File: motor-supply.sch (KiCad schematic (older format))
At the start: 16 parts, among them Q9 2N7002, U2 A8498

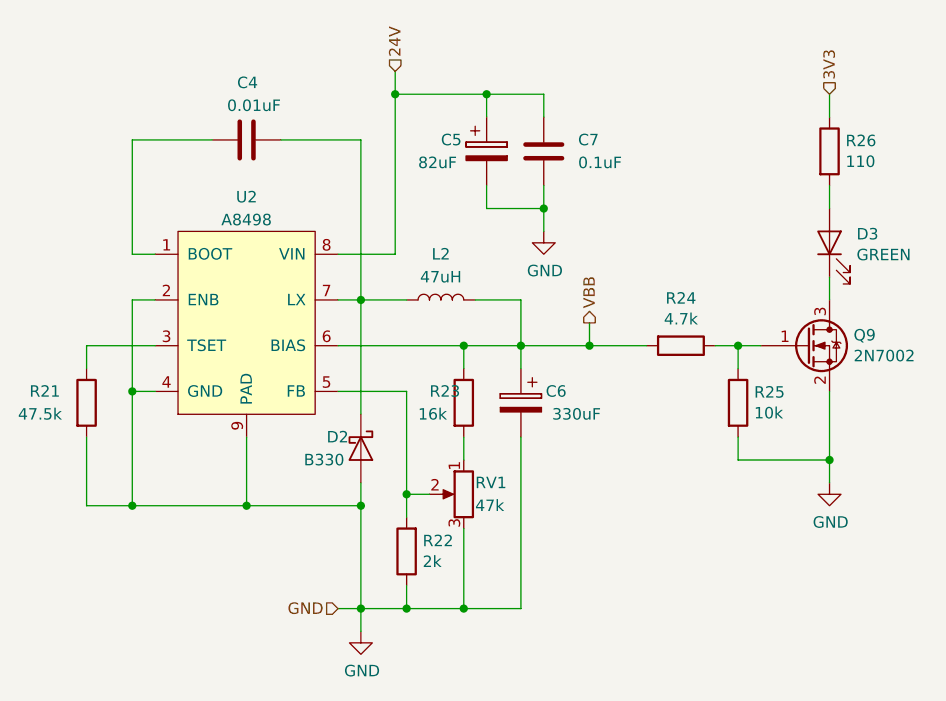
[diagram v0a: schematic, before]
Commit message: Generated annotations, netlists and assigned footprints into components
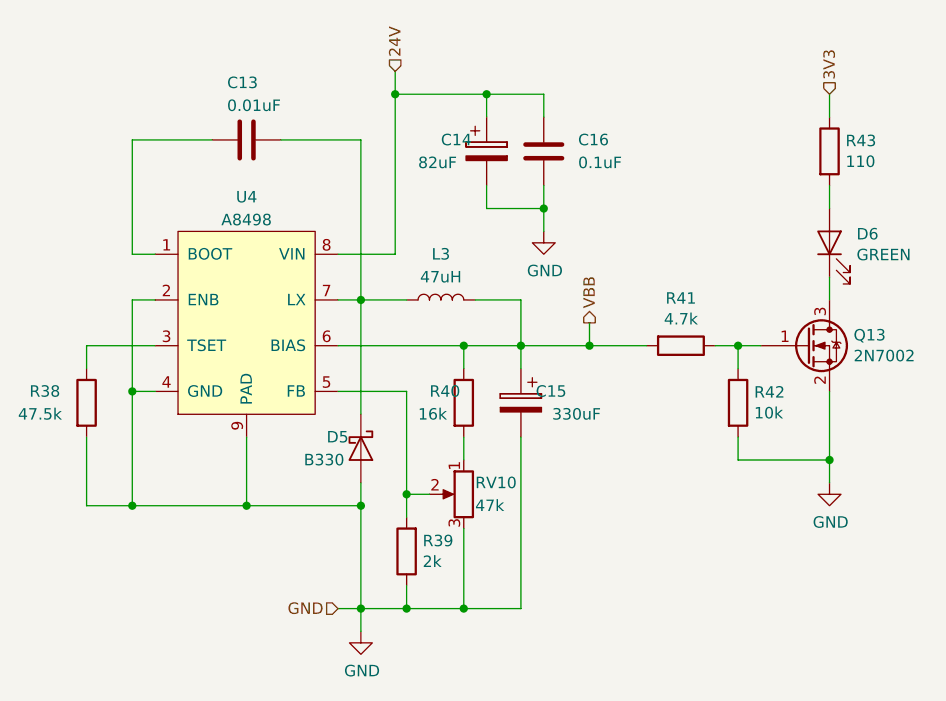
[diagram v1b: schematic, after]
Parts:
- C4: footprint (none) -> Capacitor_SMD:C_0603_1608Metric_Pad1.05x0.95mm_HandSolder
- C5: footprint (none) -> Capacitor_SMD:CP_Elec_6.3x5.8
- C6: footprint (none) -> Capacitor_SMD:CP_Elec_6.3x7.7
- C7: footprint (none) -> Capacitor_SMD:C_0805_2012Metric_Pad1.15x1.40mm_HandSolder
- D2: footprint (none) -> Diode_SMD:D_SMA_Handsoldering
- D3: footprint (none) -> LED_SMD:LED_0603_1608Metric_Pad1.05x0.95mm_HandSolder
- L2: footprint (none) -> Inductor_SMD:L_Bourns_SRP1245A
- R21, R22, R23, R25, R26: footprint (none) -> Resistor_SMD:R_0805_2012Metric_Pad1.15x1.40mm_HandSolder
- R24: footprint (none) -> Resistor_SMD:R_1206_3216Metric_Pad1.42x1.75mm_HandSolder
- RV1: footprint (none) -> Potentiometer_THT:Potentiometer_Bourns_3386P_Vertical
- U2: footprint (none) -> Package_SO:SOIC-8-1EP_3.9x4.9mm_P1.27mm_EP2.35x2.35mm
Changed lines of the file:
@@
 AR Path="/5BF2FCC4/5BDBDBC7" Ref="R?"  Part="1"
 AR Path="/5C015BBF/5BDBDBC7" Ref="R39"  Part="1"
-F 0 "R22" H 5580 4604 50  0000 R CNN
+F 0 "R39" H 5580 4604 50  0000 R CNN
 F 1 "2k" H 5580 4695 50  0000 R CNN
-F 2 "" V 5580 4650 50  0001 C CNN
+F 2 "Resistor_SMD:R_0805_2012Metric_Pad1.15x1.40mm_HandSolder" V 5580 4650 50  0001 C CNN
 F 3 "~" H 5650 4650 50  0001 C CNN
 	1    5650 4650
@@
 AR Path="/5BF2FCC4/5BDBDBCE" Ref="R?"  Part="1"
 AR Path="/5C015BBF/5BDBDBCE" Ref="R40"  Part="1"
-F 0 "R23" H 5750 4050 50  0000 L CNN
+F 0 "R40" H 5750 4050 50  0000 L CNN
 F 1 "16k" H 5700 3950 50  0000 L CNN
-F 2 "" V 5830 4000 50  0001 C CNN
+F 2 "Resistor_SMD:R_0805_2012Metric_Pad1.15x1.40mm_HandSolder" V 5830 4000 50  0001 C CNN
 F 3 "~" H 5900 4000 50  0001 C CNN
 	1    5900 4000
@@
 AR Path="/5BF2FCC4/5BDBDBD5" Ref="C?"  Part="1"
 AR Path="/5C015BBF/5BDBDBD5" Ref="C16"  Part="1"
-F 0 "C7" H 6100 2850 50  0000 R CNN
+F 0 "C16" H 6100 2850 50  0000 R CNN
 F 1 "0.1uF" H 6100 2950 50  0000 R CNN
-F 2 "" H 6288 2750 50  0001 C CNN
+F 2 "Capacitor_SMD:C_0805_2012Metric_Pad1.15x1.40mm_HandSolder" H 6288 2750 50  0001 C CNN
 F 3 "~" H 6250 2900 50  0001 C CNN
 	1    6250 2900
@@
 AR Path="/5BF2FCC4/5BDBDBDC" Ref="C?"  Part="1"
 AR Path="/5C015BBF/5BDBDBDC" Ref="C13"  Part="1"
-F 0 "C4" V 5200 2800 50  0000 L CNN
+F 0 "C13" V 5200 2800 50  0000 L CNN
 F 1 "0.01uF" V 5100 2700 50  0000 L CNN
-F 2 "" H 4988 2700 50  0001 C CNN
+F 2 "Capacitor_SMD:C_0603_1608Metric_Pad1.05x0.95mm_HandSolder" H 4988 2700 50  0001 C CNN
 F 3 "~" H 4950 2850 50  0001 C CNN
 	1    4950 2850
@@
 AR Path="/5BF2FCC4/5BDBDBE3" Ref="C?"  Part="1"
 AR Path="/5C015BBF/5BDBDBE3" Ref="C15"  Part="1"
-F 0 "C6" H 5950 4050 50  0000 L CNN
+F 0 "C15" H 5950 4050 50  0000 L CNN
 F 1 "330uF" H 5800 3950 50  0000 L CNN
-F 2 "" H 6188 3850 50  0001 C CNN
+F 2 "Capacitor_SMD:CP_Elec_6.3x7.7" H 6188 3850 50  0001 C CNN
 F 3 "~" H 6150 4000 50  0001 C CNN
 	1    6150 4000
@@
 AR Path="/5BF2FCC4/5BDBDBEB" Ref="L?"  Part="1"
 AR Path="/5C015BBF/5BDBDBEB" Ref="L3"  Part="1"
-F 0 "L2" V 6000 3550 50  0000 C CNN
+F 0 "L3" V 6000 3550 50  0000 C CNN
 F 1 "47uH" V 5900 3550 50  0000 C CNN
-F 2 "" H 5800 3550 50  0001 C CNN
+F 2 "Inductor_SMD:L_Bourns_SRP1245A" H 5800 3550 50  0001 C CNN
 F 3 "~" H 5800 3550 50  0001 C CNN
 F 4 "53mOhm" V 5800 3550 50  0001 C CNN "Resistance"
@@
 AR Path="/5BF2FCC4/5BDBDBF2" Ref="RV?"  Part="1"
 AR Path="/5C015BBF/5BDBDBF2" Ref="RV10"  Part="1"
-F 0 "RV1" H 5850 4450 50  0000 R CNN
+F 0 "RV10" H 5850 4450 50  0000 R CNN
 F 1 "47k" H 5850 4350 50  0000 R CNN
-F 2 "" H 5900 4400 50  0001 C CNN
+F 2 "Potentiometer_THT:Potentiometer_Bourns_3386P_Vertical" H 5900 4400 50  0001 C CNN
 F 3 "~" H 5900 4400 50  0001 C CNN
 	1    5900 4400
@@
 AR Path="/5BF2FCC4/5BDBDBF9" Ref="U?"  Part="1"
 AR Path="/5C015BBF/5BDBDBF9" Ref="U4"  Part="1"
-F 0 "U2" H 4950 4800 50  0000 C CNN
+F 0 "U4" H 4950 4800 50  0000 C CNN
 F 1 "A8498" H 4950 4700 50  0000 C CNN
-F 2 "" H 4800 3950 50  0001 C CNN
+F 2 "Package_SO:SOIC-8-1EP_3.9x4.9mm_P1.27mm_EP2.35x2.35mm" H 4800 3950 50  0001 C CNN
 F 3 "" H 4800 3950 50  0001 C CNN
 	1    4800 3950
@@
 AR Path="/5BF2FCC4/5BDBDC38" Ref="C?"  Part="1"
 AR Path="/5C015BBF/5BDBDC38" Ref="C14"  Part="1"
-F 0 "C5" H 5800 2950 50  0000 L CNN
+F 0 "C14" H 5800 2950 50  0000 L CNN
 F 1 "82uF" H 5700 2850 50  0000 L CNN
-F 2 "" H 6038 2750 50  0001 C CNN
+F 2 "Capacitor_SMD:CP_Elec_6.3x5.8" H 6038 2750 50  0001 C CNN
 F 3 "~" H 6000 2900 50  0001 C CNN
 	1    6000 2900
@@
 AR Path="/5BF2FCC4/5BDBDC4C" Ref="R?"  Part="1"
 AR Path="/5C015BBF/5BDBDC4C" Ref="R38"  Part="1"
-F 0 "R21" H 4000 4050 50  0000 L CNN
+F 0 "R38" H 4000 4050 50  0000 L CNN
 F 1 "47.5k" H 3950 3950 50  0000 L CNN
-F 2 "" V 4180 4000 50  0001 C CNN
+F 2 "Resistor_SMD:R_0805_2012Metric_Pad1.15x1.40mm_HandSolder" V 4180 4000 50  0001 C CNN
 F 3 "~" H 4250 4000 50  0001 C CNN
 	1    4250 4000
@@
 AR Path="/5BF2FCC4/5BDBDC5F" Ref="Q?"  Part="1"
 AR Path="/5C015BBF/5BDBDC5F" Ref="Q13"  Part="1"
-F 0 "Q9" H 7605 3796 50  0000 L CNN
+F 0 "Q13" H 7605 3796 50  0000 L CNN
 F 1 "2N7002" H 7605 3705 50  0000 L CNN
 F 2 "Package_TO_SOT_SMD:SOT-23" H 7600 3675 50  0001 L CIN
@@
 AR Path="/5BF2FCC4/5BDBDC66" Ref="R?"  Part="1"
 AR Path="/5C015BBF/5BDBDC66" Ref="R41"  Part="1"
-F 0 "R24" V 6643 3750 50  0000 C CNN
+F 0 "R41" V 6643 3750 50  0000 C CNN
 F 1 "4.7k" V 6734 3750 50  0000 C CNN
-F 2 "" V 6780 3750 50  0001 C CNN
+F 2 "Resistor_SMD:R_1206_3216Metric_Pad1.42x1.75mm_HandSolder" V 6780 3750 50  0001 C CNN
 F 3 "~" H 6850 3750 50  0001 C CNN
 	1    6850 3750
@@
 AR Path="/5BF2FCC4/5BDBDC75" Ref="D?"  Part="1"
 AR Path="/5C015BBF/5BDBDC75" Ref="D6"  Part="1"
-F 0 "D3" V 7538 3182 50  0000 R CNN
+F 0 "D6" V 7538 3182 50  0000 R CNN
 F 1 "GREEN" V 7447 3182 50  0000 R CNN
-F 2 "" H 7500 3300 50  0001 C CNN
+F 2 "LED_SMD:LED_0603_1608Metric_Pad1.05x0.95mm_HandSolder" H 7500 3300 50  0001 C CNN
 F 3 "~" H 7500 3300 50  0001 C CNN
 	1    7500 3300
@@
 AR Path="/5BF2FCC4/5BDBDC7D" Ref="R?"  Part="1"
 AR Path="/5C015BBF/5BDBDC7D" Ref="R43"  Part="1"
-F 0 "R26" H 7570 2946 50  0000 L CNN
+F 0 "R43" H 7570 2946 50  0000 L CNN
 F 1 "110" H 7570 2855 50  0000 L CNN
-F 2 "" V 7430 2900 50  0001 C CNN
+F 2 "Resistor_SMD:R_0805_2012Metric_Pad1.15x1.40mm_HandSolder" V 7430 2900 50  0001 C CNN
 F 3 "~" H 7500 2900 50  0001 C CNN
 	1    7500 2900
@@
 AR Path="/5BF2FCC4/5BDBDC88" Ref="R?"  Part="1"
 AR Path="/5C015BBF/5BDBDC88" Ref="R42"  Part="1"
-F 0 "R25" H 7170 4046 50  0000 L CNN
+F 0 "R42" H 7170 4046 50  0000 L CNN
 F 1 "10k" H 7170 3955 50  0000 L CNN
-F 2 "" V 7030 4000 50  0001 C CNN
+F 2 "Resistor_SMD:R_0805_2012Metric_Pad1.15x1.40mm_HandSolder" V 7030 4000 50  0001 C CNN
 F 3 "~" H 7100 4000 50  0001 C CNN
 	1    7100 4000
@@
 AR Path="/5BF2FCC4/5BDBDCA0" Ref="D?"  Part="1"
 AR Path="/5C015BBF/5BDBDCA0" Ref="D5"  Part="1"
-F 0 "D2" V 5400 4050 50  0000 L CNN
+F 0 "D5" V 5400 4050 50  0000 L CNN
 F 1 "B330" V 5500 3950 50  0000 L CNN
-F 2 "" H 5450 4200 50  0001 C CNN
+F 2 "Diode_SMD:D_SMA_Handsoldering" H 5450 4200 50  0001 C CNN
 F 3 "~" H 5450 4200 50  0001 C CNN
 	1    5450 4200

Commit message: Added power supply section to PCB. Added missing components footprints.
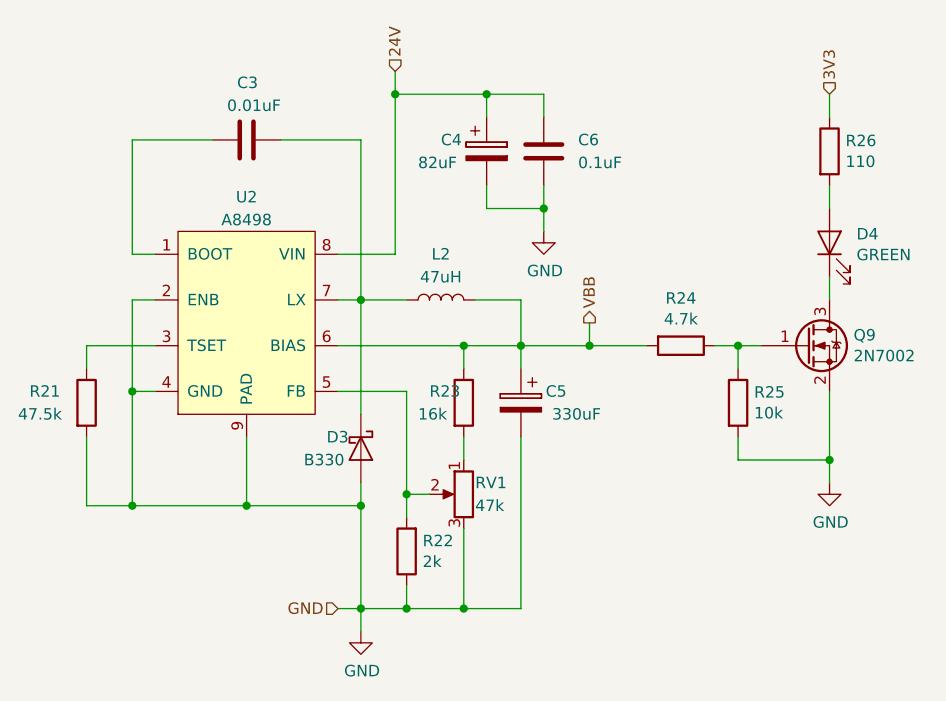
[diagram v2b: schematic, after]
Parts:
- D3: renamed from D2; footprint Diode_SMD:D_SMA_Handsoldering -> Diode_SMD:D_SMA
- Q9: footprint Package_TO_SOT_SMD:SOT-23 -> Package_TO_SOT_SMD:SOT-23_Handsoldering
- renumbered C4 to C3, C5 to C4, C6 to C5, C7 to C6, D3 to D4
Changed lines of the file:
@@
 AR Path="/5BF2FCC4/5BDBDBC7" Ref="R?"  Part="1"
 AR Path="/5C015BBF/5BDBDBC7" Ref="R39"  Part="1"
-F 0 "R39" H 5580 4604 50  0000 R CNN
+F 0 "R22" H 5580 4604 50  0000 R CNN
 F 1 "2k" H 5580 4695 50  0000 R CNN
 F 2 "Resistor_SMD:R_0805_2012Metric_Pad1.15x1.40mm_HandSolder" V 5580 4650 50  0001 C CNN
@@
 AR Path="/5BF2FCC4/5BDBDBCE" Ref="R?"  Part="1"
 AR Path="/5C015BBF/5BDBDBCE" Ref="R40"  Part="1"
-F 0 "R40" H 5750 4050 50  0000 L CNN
+F 0 "R23" H 5750 4050 50  0000 L CNN
 F 1 "16k" H 5700 3950 50  0000 L CNN
 F 2 "Resistor_SMD:R_0805_2012Metric_Pad1.15x1.40mm_HandSolder" V 5830 4000 50  0001 C CNN
@@
 $EndComp
 $Comp
-L Device:C C7
+L Device:C C6
 U 1 1 5BDBDBD5
 P 6250 2900
-AR Path="/5BDCD47C/5BDBDBD5" Ref="C7"  Part="1"
+AR Path="/5BDCD47C/5BDBDBD5" Ref="C6"  Part="1"
 AR Path="/5BF2FCC4/5BDBDBD5" Ref="C?"  Part="1"
-AR Path="/5C015BBF/5BDBDBD5" Ref="C16"  Part="1"
-F 0 "C16" H 6100 2850 50  0000 R CNN
+AR Path="/5C015BBF/5BDBDBD5" Ref="C15"  Part="1"
+F 0 "C6" H 6100 2850 50  0000 R CNN
 F 1 "0.1uF" H 6100 2950 50  0000 R CNN
 F 2 "Capacitor_SMD:C_0805_2012Metric_Pad1.15x1.40mm_HandSolder" H 6288 2750 50  0001 C CNN
@@
 $EndComp
 $Comp
-L Device:C C4
+L Device:C C3
 U 1 1 5BDBDBDC
 P 4950 2850
-AR Path="/5BDCD47C/5BDBDBDC" Ref="C4"  Part="1"
+AR Path="/5BDCD47C/5BDBDBDC" Ref="C3"  Part="1"
 AR Path="/5BF2FCC4/5BDBDBDC" Ref="C?"  Part="1"
-AR Path="/5C015BBF/5BDBDBDC" Ref="C13"  Part="1"
-F 0 "C13" V 5200 2800 50  0000 L CNN
+AR Path="/5C015BBF/5BDBDBDC" Ref="C12"  Part="1"
+F 0 "C3" V 5200 2800 50  0000 L CNN
 F 1 "0.01uF" V 5100 2700 50  0000 L CNN
 F 2 "Capacitor_SMD:C_0603_1608Metric_Pad1.05x0.95mm_HandSolder" H 4988 2700 50  0001 C CNN
@@
 $EndComp
 $Comp
-L Device:CP C6
+L Device:CP C5
 U 1 1 5BDBDBE3
 P 6150 4000
-AR Path="/5BDCD47C/5BDBDBE3" Ref="C6"  Part="1"
+AR Path="/5BDCD47C/5BDBDBE3" Ref="C5"  Part="1"
 AR Path="/5BF2FCC4/5BDBDBE3" Ref="C?"  Part="1"
-AR Path="/5C015BBF/5BDBDBE3" Ref="C15"  Part="1"
-F 0 "C15" H 5950 4050 50  0000 L CNN
+AR Path="/5C015BBF/5BDBDBE3" Ref="C14"  Part="1"
+F 0 "C5" H 5950 4050 50  0000 L CNN
 F 1 "330uF" H 5800 3950 50  0000 L CNN
 F 2 "Capacitor_SMD:CP_Elec_6.3x7.7" H 6188 3850 50  0001 C CNN
@@
 AR Path="/5BF2FCC4/5BDBDBEB" Ref="L?"  Part="1"
 AR Path="/5C015BBF/5BDBDBEB" Ref="L3"  Part="1"
-F 0 "L3" V 6000 3550 50  0000 C CNN
+F 0 "L2" V 6000 3550 50  0000 C CNN
 F 1 "47uH" V 5900 3550 50  0000 C CNN
 F 2 "Inductor_SMD:L_Bourns_SRP1245A" H 5800 3550 50  0001 C CNN
@@
 AR Path="/5BF2FCC4/5BDBDBF2" Ref="RV?"  Part="1"
 AR Path="/5C015BBF/5BDBDBF2" Ref="RV10"  Part="1"
-F 0 "RV10" H 5850 4450 50  0000 R CNN
+F 0 "RV1" H 5850 4450 50  0000 R CNN
 F 1 "47k" H 5850 4350 50  0000 R CNN
 F 2 "Potentiometer_THT:Potentiometer_Bourns_3386P_Vertical" H 5900 4400 50  0001 C CNN
@@
 AR Path="/5BF2FCC4/5BDBDBF9" Ref="U?"  Part="1"
 AR Path="/5C015BBF/5BDBDBF9" Ref="U4"  Part="1"
-F 0 "U4" H 4950 4800 50  0000 C CNN
+F 0 "U2" H 4950 4800 50  0000 C CNN
 F 1 "A8498" H 4950 4700 50  0000 C CNN
 F 2 "Package_SO:SOIC-8-1EP_3.9x4.9mm_P1.27mm_EP2.35x2.35mm" H 4800 3950 50  0001 C CNN
@@
 	5900 3750 6150 3750
 $Comp
-L power:GND #PWR012
+L power:GND #PWR06
 U 1 1 5BDBDC17
 P 6250 3250
-AR Path="/5BDCD47C/5BDBDC17" Ref="#PWR012"  Part="1"
+AR Path="/5BDCD47C/5BDBDC17" Ref="#PWR06"  Part="1"
 AR Path="/5BF2FCC4/5BDBDC17" Ref="#PWR?"  Part="1"
-AR Path="/5C015BBF/5BDBDC17" Ref="#PWR020"  Part="1"
-F 0 "#PWR020" H 6250 3000 50  0001 C CNN
+AR Path="/5C015BBF/5BDBDC17" Ref="#PWR012"  Part="1"
+F 0 "#PWR012" H 6250 3000 50  0001 C CNN
 F 1 "GND" H 6255 3077 50  0000 C CNN
 F 2 "" H 6250 3250 50  0001 C CNN
@@
 P 5450 5000
 AR Path="/5BDB64FF/5BDBDC1D" Ref="#PWR?"  Part="1"
-AR Path="/5BDCD47C/5BDBDC1D" Ref="#PWR010"  Part="1"
+AR Path="/5BDCD47C/5BDBDC1D" Ref="#PWR05"  Part="1"
 AR Path="/5BF2FCC4/5BDBDC1D" Ref="#PWR?"  Part="1"
-AR Path="/5C015BBF/5BDBDC1D" Ref="#PWR018"  Part="1"
-F 0 "#PWR018" H 5450 4750 50  0001 C CNN
+AR Path="/5C015BBF/5BDBDC1D" Ref="#PWR011"  Part="1"
+F 0 "#PWR011" H 5450 4750 50  0001 C CNN
 F 1 "GND" H 5455 4827 50  0000 C CNN
 F 2 "" H 5450 5000 50  0001 C CNN
@@
 Connection ~ 4450 3950
 $Comp
-L Device:CP C5
+L Device:CP C4
 U 1 1 5BDBDC38
 P 6000 2900
-AR Path="/5BDCD47C/5BDBDC38" Ref="C5"  Part="1"
+AR Path="/5BDCD47C/5BDBDC38" Ref="C4"  Part="1"
 AR Path="/5BF2FCC4/5BDBDC38" Ref="C?"  Part="1"
-AR Path="/5C015BBF/5BDBDC38" Ref="C14"  Part="1"
-F 0 "C14" H 5800 2950 50  0000 L CNN
+AR Path="/5C015BBF/5BDBDC38" Ref="C13"  Part="1"
+F 0 "C4" H 5800 2950 50  0000 L CNN
 F 1 "82uF" H 5700 2850 50  0000 L CNN
 F 2 "Capacitor_SMD:CP_Elec_6.3x5.8" H 6038 2750 50  0001 C CNN
@@
 AR Path="/5BF2FCC4/5BDBDC4C" Ref="R?"  Part="1"
 AR Path="/5C015BBF/5BDBDC4C" Ref="R38"  Part="1"
-F 0 "R38" H 4000 4050 50  0000 L CNN
+F 0 "R21" H 4000 4050 50  0000 L CNN
 F 1 "47.5k" H 3950 3950 50  0000 L CNN
 F 2 "Resistor_SMD:R_0805_2012Metric_Pad1.15x1.40mm_HandSolder" V 4180 4000 50  0001 C CNN
@@
 AR Path="/5BF2FCC4/5BDBDC5F" Ref="Q?"  Part="1"
 AR Path="/5C015BBF/5BDBDC5F" Ref="Q13"  Part="1"
-F 0 "Q13" H 7605 3796 50  0000 L CNN
+F 0 "Q9" H 7605 3796 50  0000 L CNN
 F 1 "2N7002" H 7605 3705 50  0000 L CNN
-F 2 "Package_TO_SOT_SMD:SOT-23" H 7600 3675 50  0001 L CIN
+F 2 "Package_TO_SOT_SMD:SOT-23_Handsoldering" H 7600 3675 50  0001 L CIN
 F 3 "https://www.fairchildsemi.com/datasheets/2N/2N7002.pdf" H 7400 3750 50  0001 L CNN
 	1    7400 3750
@@
 AR Path="/5BF2FCC4/5BDBDC66" Ref="R?"  Part="1"
 AR Path="/5C015BBF/5BDBDC66" Ref="R41"  Part="1"
-F 0 "R41" V 6643 3750 50  0000 C CNN
+F 0 "R24" V 6643 3750 50  0000 C CNN
 F 1 "4.7k" V 6734 3750 50  0000 C CNN
 F 2 "Resistor_SMD:R_1206_3216Metric_Pad1.42x1.75mm_HandSolder" V 6780 3750 50  0001 C CNN
@@
 $EndComp
 $Comp
-L power:GND #PWR013
+L power:GND #PWR07
 U 1 1 5BDBDC6D
 P 7500 4350
-AR Path="/5BDCD47C/5BDBDC6D" Ref="#PWR013"  Part="1"
+AR Path="/5BDCD47C/5BDBDC6D" Ref="#PWR07"  Part="1"
 AR Path="/5BF2FCC4/5BDBDC6D" Ref="#PWR?"  Part="1"
-AR Path="/5C015BBF/5BDBDC6D" Ref="#PWR021"  Part="1"
-F 0 "#PWR021" H 7500 4100 50  0001 C CNN
+AR Path="/5C015BBF/5BDBDC6D" Ref="#PWR013"  Part="1"
+F 0 "#PWR013" H 7500 4100 50  0001 C CNN
 F 1 "GND" H 7505 4177 50  0000 C CNN
 F 2 "" H 7500 4350 50  0001 C CNN
@@
 	7200 3750 7100 3750
 $Comp
-L Device:LED D3
+L Device:LED D4
 U 1 1 5BDBDC75
 P 7500 3300
-AR Path="/5BDCD47C/5BDBDC75" Ref="D3"  Part="1"
+AR Path="/5BDCD47C/5BDBDC75" Ref="D4"  Part="1"
 AR Path="/5BF2FCC4/5BDBDC75" Ref="D?"  Part="1"
-AR Path="/5C015BBF/5BDBDC75" Ref="D6"  Part="1"
-F 0 "D6" V 7538 3182 50  0000 R CNN
+AR Path="/5C015BBF/5BDBDC75" Ref="D7"  Part="1"
+F 0 "D4" V 7538 3182 50  0000 R CNN
 F 1 "GREEN" V 7447 3182 50  0000 R CNN
 F 2 "LED_SMD:LED_0603_1608Metric_Pad1.05x0.95mm_HandSolder" H 7500 3300 50  0001 C CNN
@@
 AR Path="/5BF2FCC4/5BDBDC7D" Ref="R?"  Part="1"
 AR Path="/5C015BBF/5BDBDC7D" Ref="R43"  Part="1"
-F 0 "R43" H 7570 2946 50  0000 L CNN
+F 0 "R26" H 7570 2946 50  0000 L CNN
 F 1 "110" H 7570 2855 50  0000 L CNN
 F 2 "Resistor_SMD:R_0805_2012Metric_Pad1.15x1.40mm_HandSolder" V 7430 2900 50  0001 C CNN
@@
 AR Path="/5BF2FCC4/5BDBDC88" Ref="R?"  Part="1"
 AR Path="/5C015BBF/5BDBDC88" Ref="R42"  Part="1"
-F 0 "R42" H 7170 4046 50  0000 L CNN
+F 0 "R25" H 7170 4046 50  0000 L CNN
 F 1 "10k" H 7170 3955 50  0000 L CNN
 F 2 "Resistor_SMD:R_0805_2012Metric_Pad1.15x1.40mm_HandSolder" V 7030 4000 50  0001 C CNN
@@
 	6150 3750 6150 3850
 $Comp
-L Device:D_Schottky D2
+L Device:D_Schottky D3
 U 1 1 5BDBDCA0
 P 5450 4200
-AR Path="/5BDCD47C/5BDBDCA0" Ref="D2"  Part="1"
+AR Path="/5BDCD47C/5BDBDCA0" Ref="D3"  Part="1"
 AR Path="/5BF2FCC4/5BDBDCA0" Ref="D?"  Part="1"
-AR Path="/5C015BBF/5BDBDCA0" Ref="D5"  Part="1"
-F 0 "D5" V 5400 4050 50  0000 L CNN
+AR Path="/5C015BBF/5BDBDCA0" Ref="D6"  Part="1"
+F 0 "D3" V 5400 4050 50  0000 L CNN
 F 1 "B330" V 5500 3950 50  0000 L CNN
-F 2 "Diode_SMD:D_SMA_Handsoldering" H 5450 4200 50  0001 C CNN
+F 2 "Diode_SMD:D_SMA" H 5450 4200 50  0001 C CNN
 F 3 "~" H 5450 4200 50  0001 C CNN
 	1    5450 4200
